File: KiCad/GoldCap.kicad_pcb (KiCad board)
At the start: 2 copper layers, 38.1 x 35.6 mm, 43 parts, among them J1 Pwr In, J2 Pwr Out, J3 Main Pwr, J4 Prog, J5 Conn_01x09_Male, Q1 BC847, Q2 IRLML6401, SW1 SW_TACTILE_SPST, U1 TPS70933DBV, U2 ATtiny20-SSU

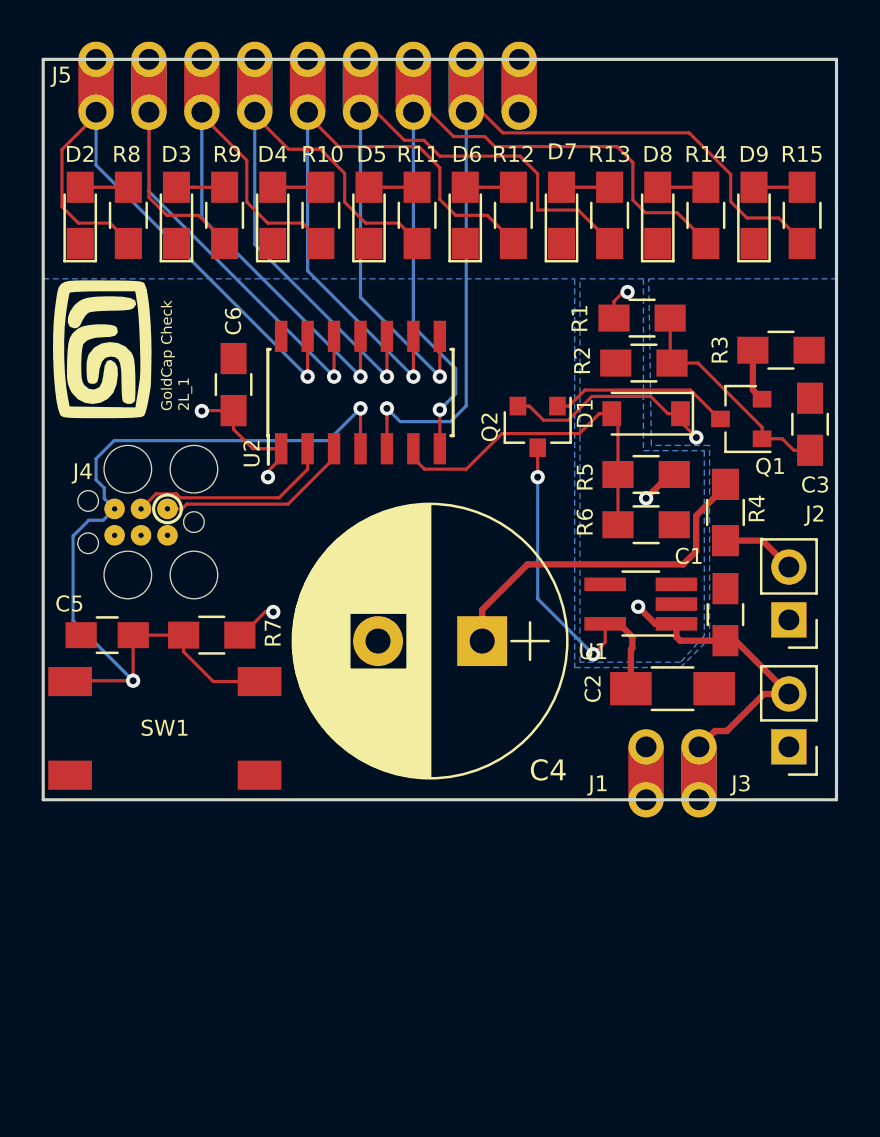
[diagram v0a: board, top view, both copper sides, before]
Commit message: Fixes the labelling and adds a breakout for the 3v3 line
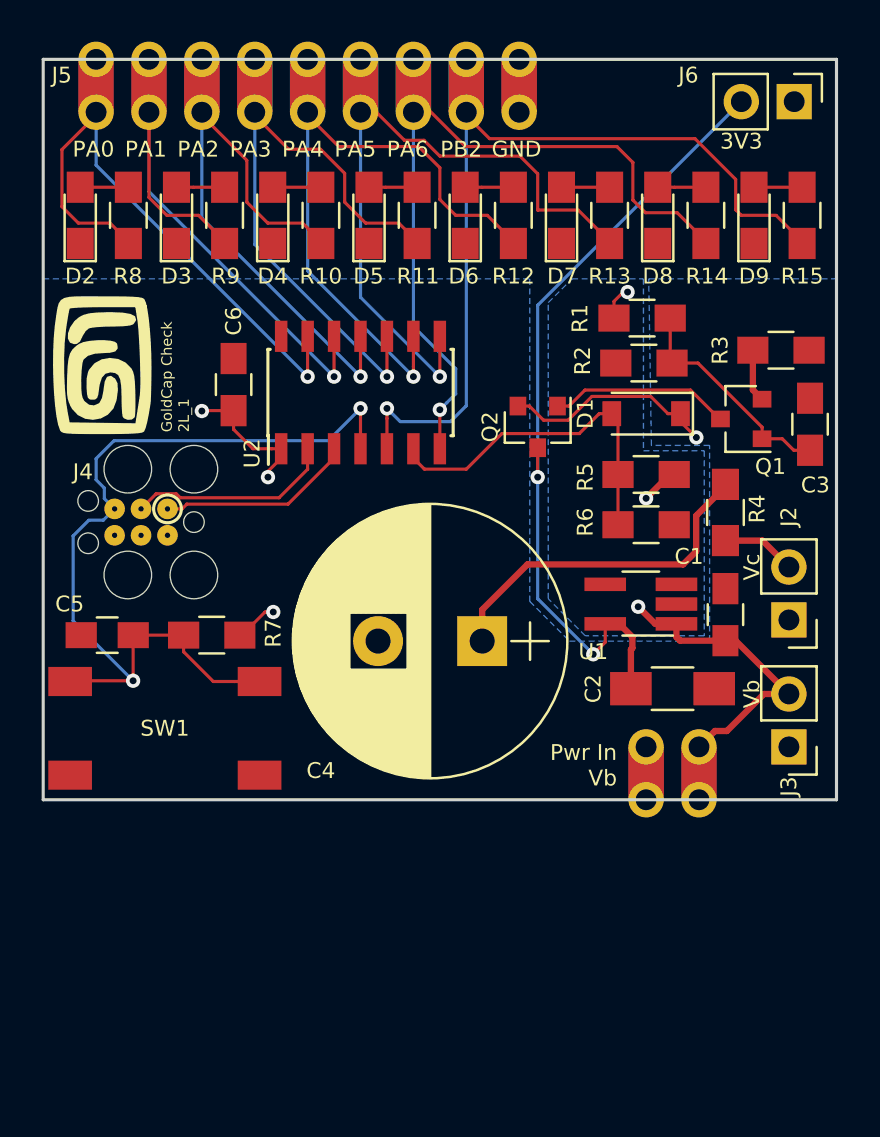
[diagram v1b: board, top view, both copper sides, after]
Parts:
- added J6: Main Pwr, Pin_Headers:Pin_Header_Straight_1x02_Pitch2.54mm, F.Cu at (86.9, 30.0)
- moved LG 0.76 mm to (53.6, 42.7)
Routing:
- net /3V3: track 16.8 -> 38.9 mm
- net /LED_PB2: track 42.1 -> 43.2 mm
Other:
- board text added: "3V3"
- board text added: "GND"
- board text added: "PA0"
- board text added: "PA0 PA1 PA2 PA3 PA4 PA5 PA6 PB2 GND"
- board text added: "PA1"
- board text added: "PA2"
- board text added: "PA3"
- board text added: "PA4"
- board text added: "PA5"
- board text added: "PA6"
- board text added: "PB2"
- board text added: "Pwr IN Vb"
- board text added: "Pwr In Vb"
- board text added: "Vb"
- board text added: "Vc"

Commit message: Created Rev 2 with the corrected GoldCap FP and a USB B Micro
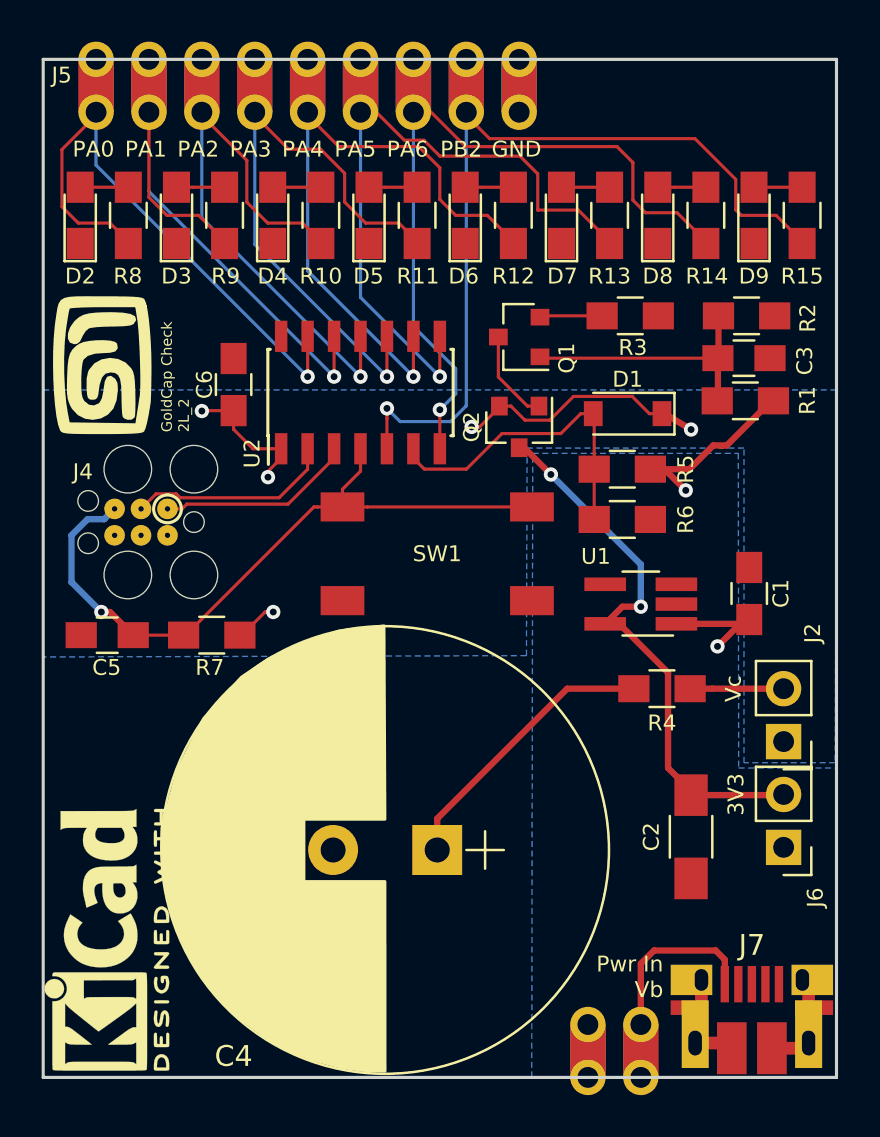
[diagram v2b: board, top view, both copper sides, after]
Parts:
- removed J3: Main Pwr, Pin_Headers:Pin_Header_Straight_1x02_Pitch2.54mm
- removed the REF*** at (69.8, 45.7)
- added J7: ~, GoldCap-Check:USB_B_2.0_Micro, F.Cu at (84.8, 75.2)
- added REF***: KiCad-Logo2_6mm_SilkScreen, Symbols:KiCad-Logo2_6mm_SilkScreen, B.Cu at (65.6, 53.3)
- added REF***: KiCad-Logo2_6mm_SilkScreen, Symbols:KiCad-Logo2_6mm_SilkScreen, F.Cu at (53.8, 70.2)
- C4: footprint Capacitors_ThroughHole:CP_Radial_D13.0mm_P5.00mm -> GoldCap-Check:CP_Radial_D21.5mm_P5.00mm
- moved J6 35.8 mm to (86.4, 65.8), turned to 180 degrees
- moved SW1 15.5 mm to (69.7, 51.7)
- moved J1 13.6 mm to (79.5, 74.3)
- moved Q1 11.4 mm to (73.7, 41.3)
- moved C4 10.3 mm to (69.7, 65.9)
- moved R4 8.99 mm to (80.5, 58.2), turned to 180 degrees
- moved G*** 8.61 mm to (73.9, 56.6)
- moved R3 7.42 mm to (79.0, 40.3)
- moved C2 7.17 mm to (81.9, 65.3), turned to 270 degrees
- moved R1 6.35 mm to (84.5, 44.3), turned to 0 degrees
- moved J2 5.85 mm to (86.4, 60.7)
- moved R2 5.43 mm to (84.6, 40.3), turned to 0 degrees
- moved C3 4.49 mm to (84.5, 42.3), turned to 0 degrees
- moved C1 1.53 mm to (84.7, 53.6)
- moved R6 1.17 mm to (78.6, 50.0)
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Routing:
- net /3V3: track 38.9 -> 27.0 mm
- net GND: track 0.00 -> 10.0 mm
- net /~RESET: track 42.5 -> 33.7 mm, vias 2 -> 1
- net /Vb: track 18.2 -> 24.9 mm, vias 3 -> 2
- net Net-(Q1-Pad3): track 8.72 -> 4.45 mm
- net /Vc: track 22.7 -> 26.0 mm, vias 4 -> 5
- net Net-(C4-Pad1): track 16.7 -> 13.5 mm
- net Net-(C3-Pad1): track 10.9 -> 12.7 mm
- net /PwrMon: track 16.8 -> 15.9 mm
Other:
- board size 38.1 x 35.6 mm -> 38.1 x 48.9 mm
- board text added: "GoldCap Check 2L_2"
- board text removed: "GoldCap Check 2L_1"
- board text removed: "Vb"

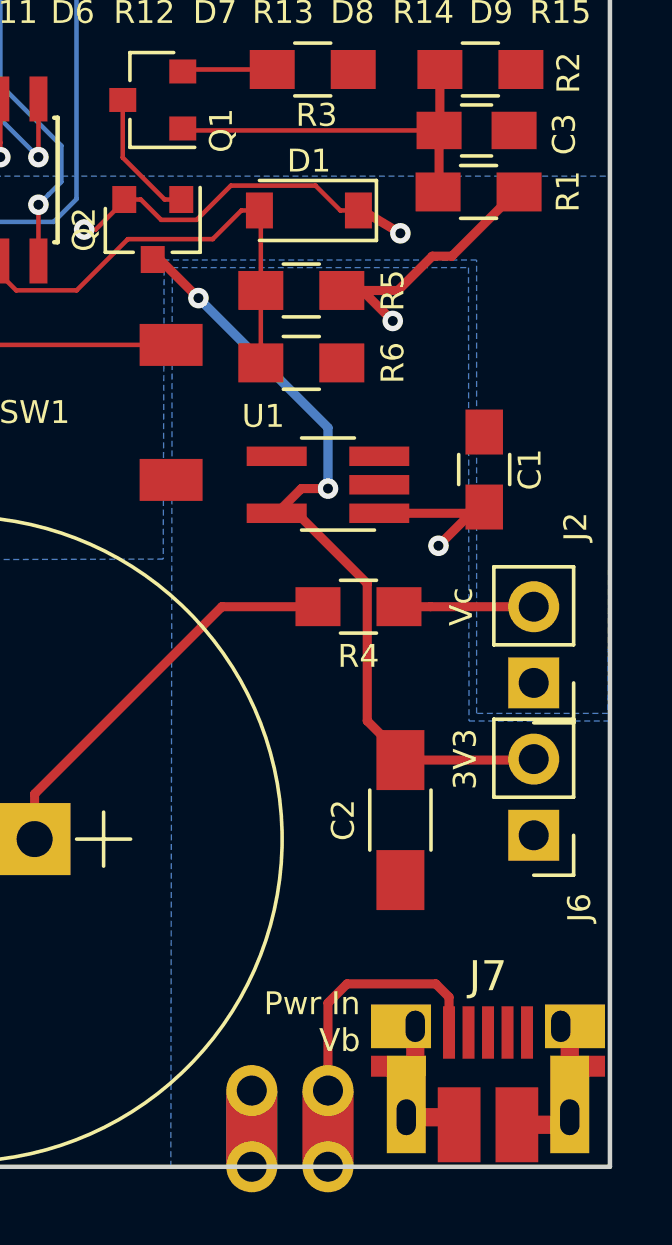
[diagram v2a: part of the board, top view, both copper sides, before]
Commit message: Adds the PRG/RUN jumper for programming in 5V
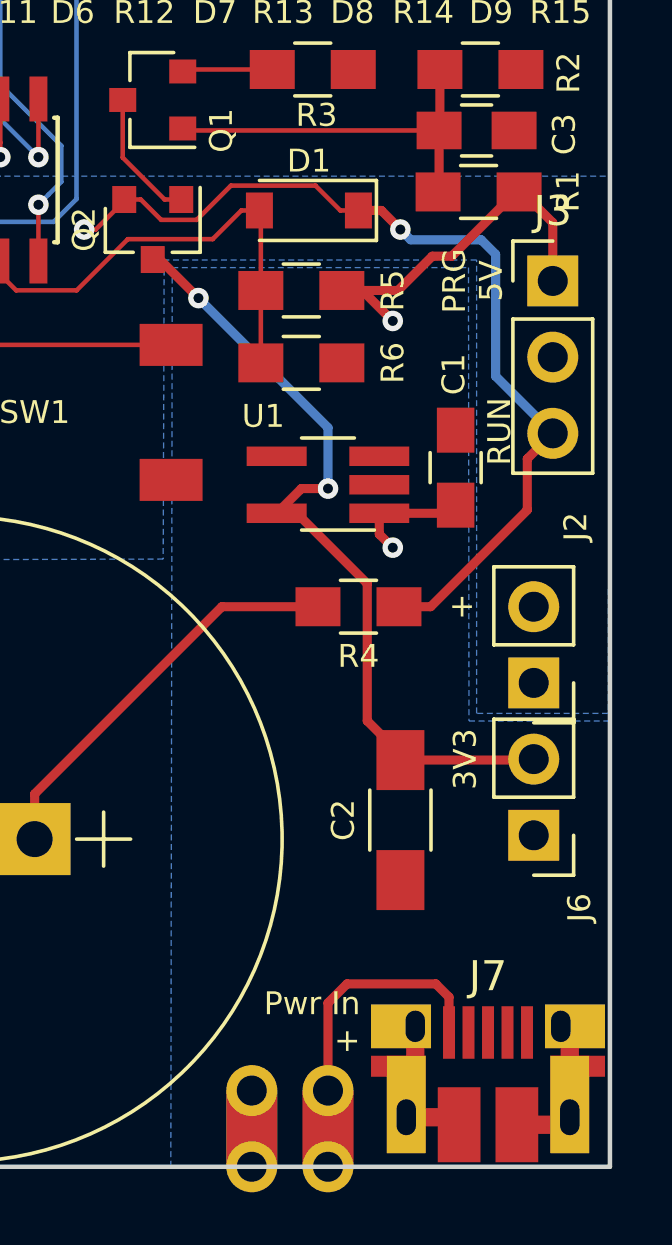
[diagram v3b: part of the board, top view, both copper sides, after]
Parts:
- added J3: Prog Jumper, Pin_Headers:Pin_Header_Straight_1x03_Pitch2.54mm, F.Cu at (87.0, 47.3)
- moved C1 0.95 mm to (83.8, 53.5)
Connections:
- D1 pad 1: /Vc -> /Vg
- Q2 pad 2: /Vc -> /Vg
- R4 pad 1: /Vc -> /Vg
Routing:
- net /Vg: track 0.00 -> 31.1 mm, vias 0 -> 2
- net /Vc: track 26.0 -> 8.80 mm, vias 5 -> 3
- net /Vb: track 24.9 -> 26.7 mm
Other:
- board text added: "+"
- board text added: "PRG 5V"
- board text added: "Pwr IN +"
- board text added: "Pwr In +"
- board text added: "RUN"
- board text removed: "Pwr IN Vb"
- board text removed: "Pwr In Vb"
- board text removed: "Vc"

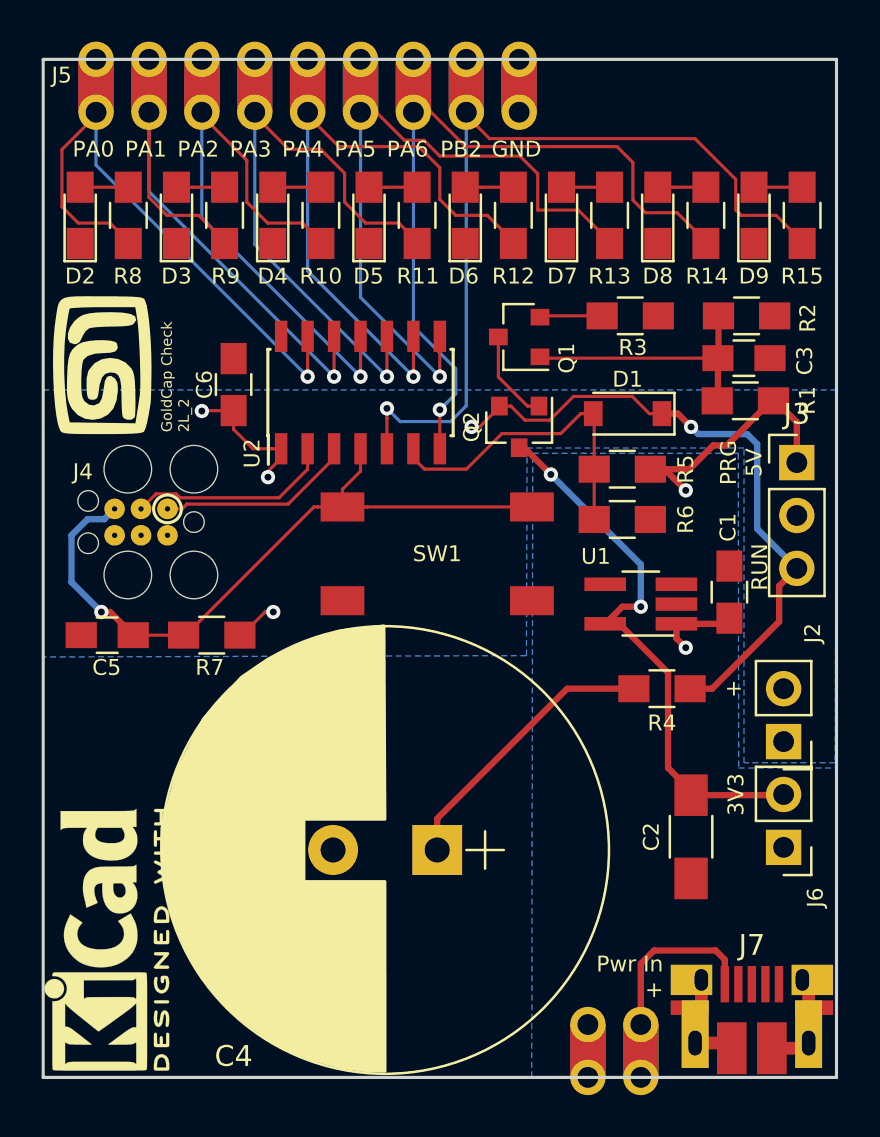
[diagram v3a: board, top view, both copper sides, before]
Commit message: Changes the handsolder 0805 to normal and neatens up labelling
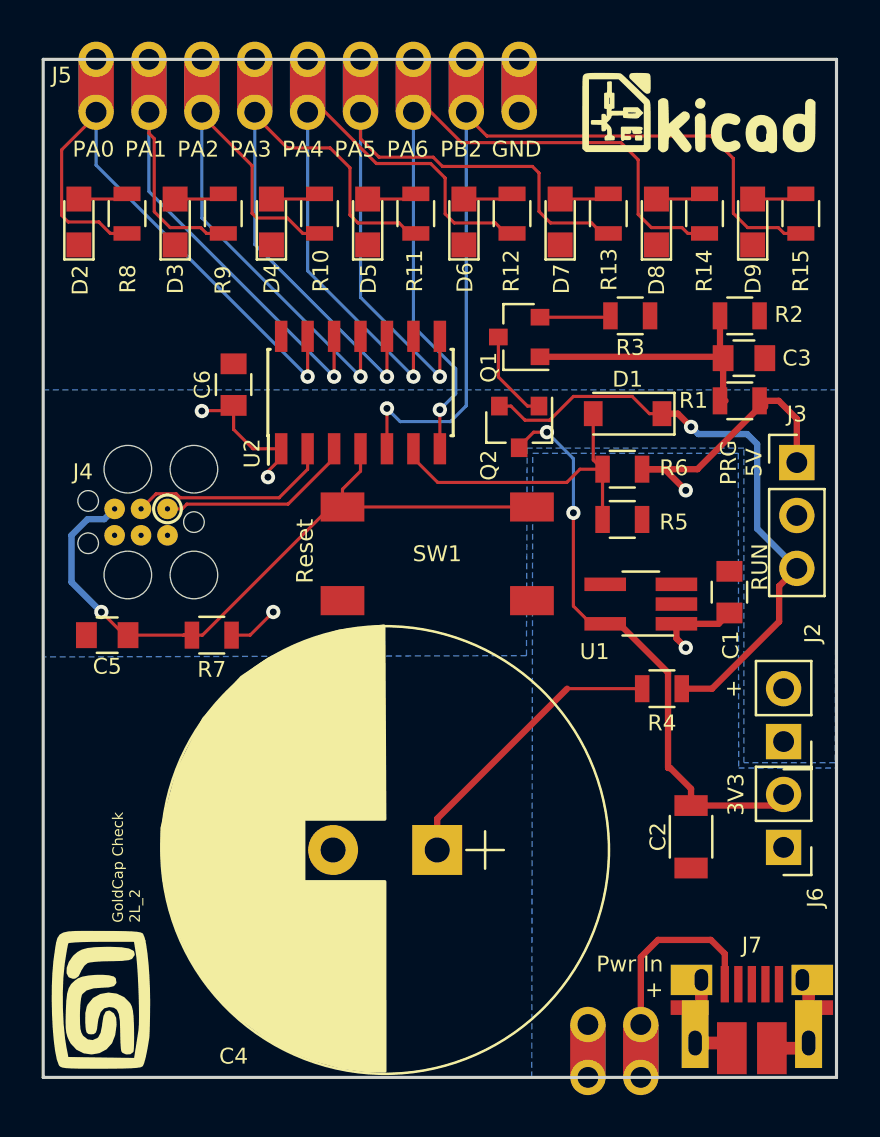
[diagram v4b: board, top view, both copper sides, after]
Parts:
- removed the REF*** at (53.8, 70.2)
- added ?: , GoldCap-Check:KiCad-Logo, F.Cu at (82.3, 30.5)
- C1, C3, C5, C6: footprint Capacitors_SMD:C_0805_HandSoldering -> Capacitors_SMD:C_0805
- C2: footprint Capacitors_SMD:C_1206_HandSoldering -> Capacitors_SMD:C_1206
- D2, D3, D4, D5, D6, D7, D8, D9: footprint LEDs:LED_0805_HandSoldering -> LEDs:LED_0805
- R1, R10, R11, R12, R13, R14, R15, R2, R3, R4, R5, R6, R7, R8, R9: footprint Resistors_SMD:R_0805_HandSoldering -> Resistors_SMD:R_0805
- moved LG 30.5 mm to (53.5, 73.2)
- moved R2 0.33 mm to (84.3, 40.3)
- moved D2 0.32 mm to (52.5, 35.8)
- moved D8 0.32 mm to (80.3, 35.8)
- moved D9 0.32 mm to (84.9, 35.8)
- moved D3 0.32 mm to (57.1, 35.8)
- moved D4 0.32 mm to (61.8, 35.8)
- moved D5 0.32 mm to (66.4, 35.8)
- moved D6 0.32 mm to (71.0, 35.8)
- moved D7 0.32 mm to (75.6, 35.8)
- moved R1 0.27 mm to (84.3, 44.3)
- moved R10 0.10 mm to (64.1, 35.4)
- moved R11 0.10 mm to (68.7, 35.4)
- moved R12 0.10 mm to (73.3, 35.4)
- moved R13 0.10 mm to (77.9, 35.4)
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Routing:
- net /Vb: track 26.7 -> 29.0 mm
- net /LED_PA5: track 35.2 -> 37.3 mm
- net /LED_PA1: track 30.8 -> 29.5 mm
- net /Vg: track 31.1 -> 29.8 mm, vias 2 -> 1
- net /LED_PA6: track 38.4 -> 37.3 mm
- net /3V3: track 27.0 -> 28.0 mm
- net /LED_PA3: track 31.2 -> 30.5 mm
- net /LED_PA4: track 34.6 -> 34.0 mm
- net Net-(C3-Pad1): track 12.7 -> 13.2 mm
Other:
- board text added: "Reset"

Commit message: Changed the SOT-23_5 to reflect the datasheet
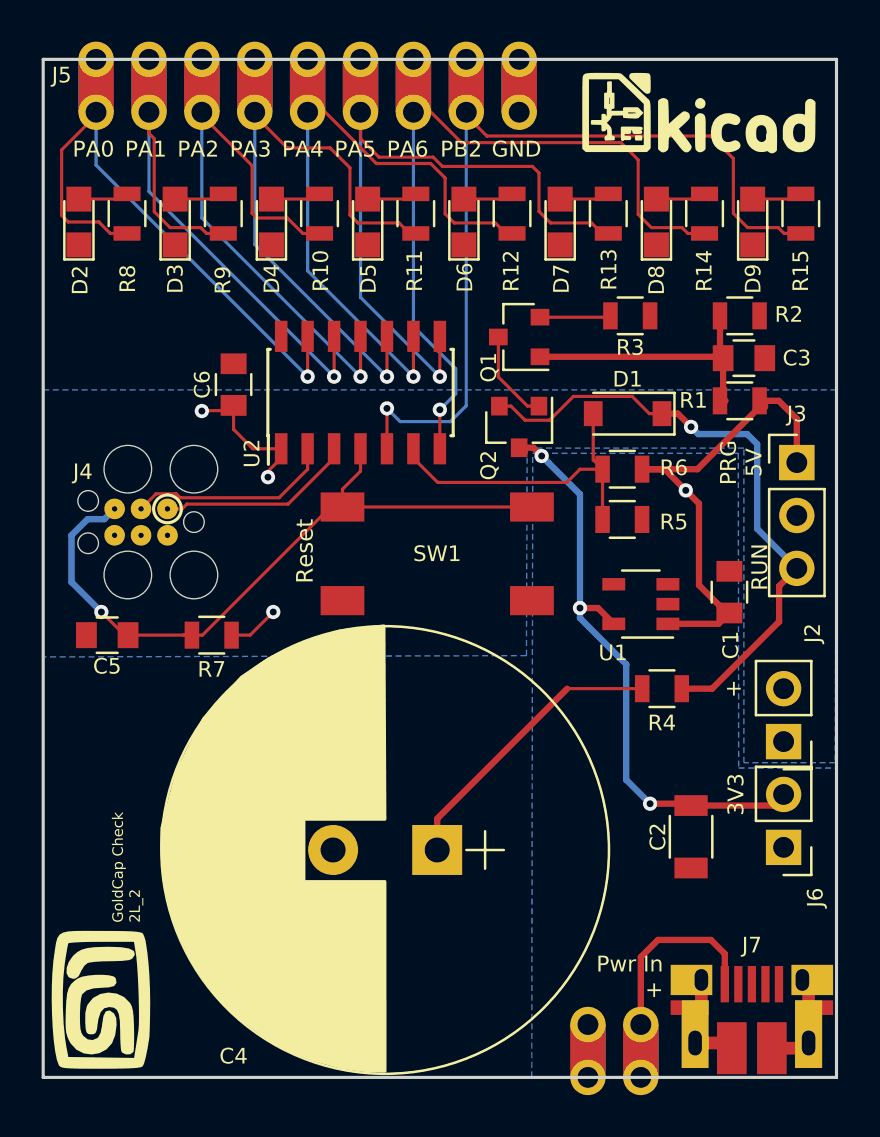
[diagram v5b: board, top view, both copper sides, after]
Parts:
- U1: footprint TO_SOT_Packages_SMD:TSOT-23-5_HandSoldering -> GoldCap-Check:SOT-23-5_TPS70933DBVR
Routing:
- net /Vb: track 29.0 -> 34.9 mm, vias 2 -> 1
- net /3V3: track 28.0 -> 28.8 mm, vias 2 -> 3
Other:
- board text added: "In Programming Mode, do not exceed 5V"
